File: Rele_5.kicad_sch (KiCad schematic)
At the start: 5 parts

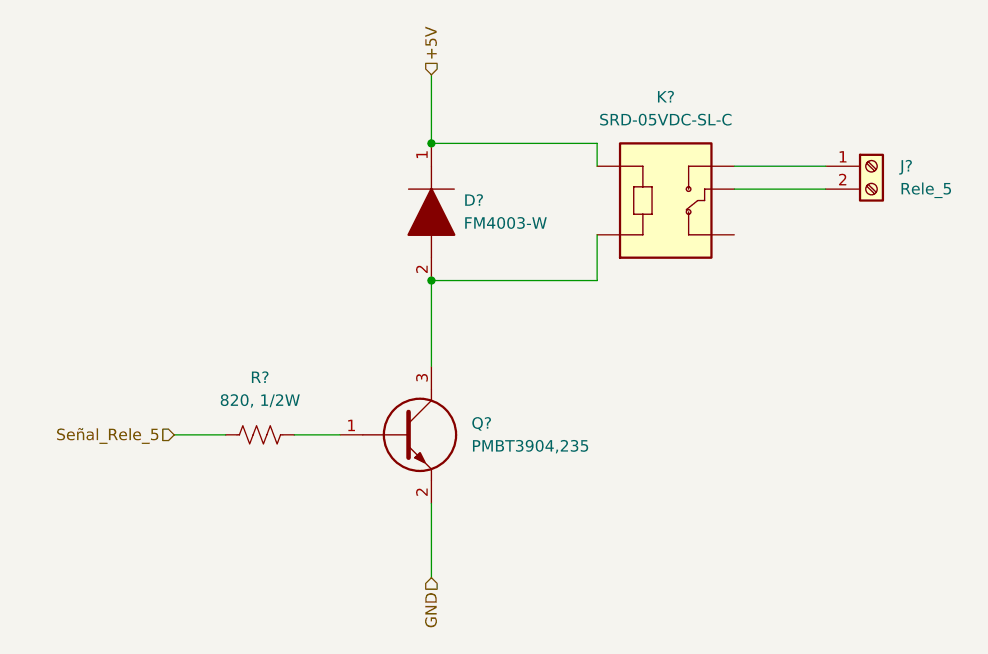
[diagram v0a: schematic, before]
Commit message: Ajuste del esquematico
Se cambio el integrado ESP32 por 2 tiras de pines de 1x15, se quitaron los switches EN y BOOT que ya estan en el NodeMCU, se quito el mutliplexor 74HC y se cablearon las I/O
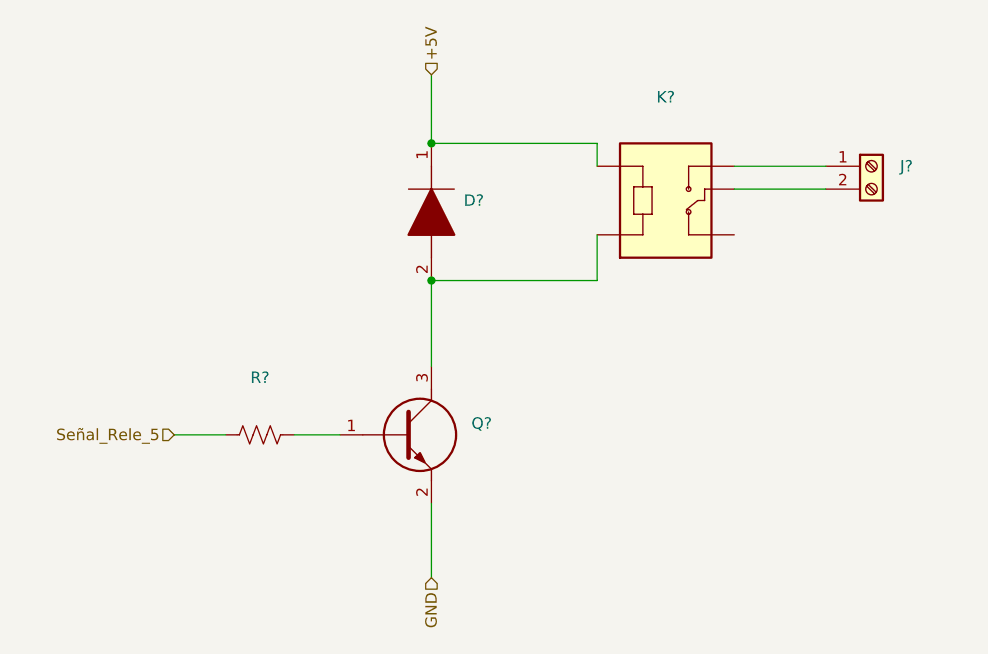
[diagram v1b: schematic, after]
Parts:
- D?: value FM4003-W -> (none); footprint DIOM5025X231N -> (none)
- J?: value Rele_5 -> (none)
- K?: value SRD-05VDC-SL-C -> (none); footprint RELAY_SRD-05VDC-SL-C -> (none)
- Q?: value PMBT3904,235 -> (none); footprint SOT95P230X110-3N -> (none)
- R?: value 820, 1/2W -> (none)
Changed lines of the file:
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@@
     (in_bom yes) (on_board yes) (fields_autoplaced)
     (property "Reference" "K?" (id 0) (at 169.545 70.4342 0))
-    (property "Value" "SRD-05VDC-SL-C" (id 1) (at 169.545 72.9742 0))
-    (property "Footprint" "RELAY_SRD-05VDC-SL-C" (id 2) (at 169.545 80.645 0)
+    (property "Value" "" (id 1) (at 169.545 72.9742 0))
+    (property "Footprint" "" (id 2) (at 169.545 80.645 0)
       (effects (font (size 1.27 1.27)) (justify left bottom) hide)
     )
@@
       (effects (font (size 1.27 1.27)) (justify left))
     )
-    (property "Value" "PMBT3904,235" (id 1) (at 147.955 109.2199 0)
+    (property "Value" "" (id 1) (at 147.955 109.2199 0)
       (effects (font (size 1.27 1.27)) (justify left))
     )
-    (property "Footprint" "SOT95P230X110-3N" (id 2) (at 147.32 111.76 0)
+    (property "Footprint" "" (id 2) (at 147.32 111.76 0)
       (effects (font (size 1.27 1.27)) (justify left) hide)
     )
@@
     (in_bom yes) (on_board yes) (fields_autoplaced)
     (property "Reference" "R?" (id 0) (at 124.46 101.6 90))
-    (property "Value" "820, 1/2W" (id 1) (at 124.46 104.14 90))
+    (property "Value" "" (id 1) (at 124.46 104.14 90))
     (property "Footprint" "" (id 2) (at 124.714 106.934 90)
       (effects (font (size 1.27 1.27)) hide)
@@
       (effects (font (size 1.27 1.27)) (justify left))
     )
-    (property "Value" "Rele_5" (id 1) (at 195.58 80.6449 0)
+    (property "Value" "" (id 1) (at 195.58 80.6449 0)
       (effects (font (size 1.27 1.27)) (justify left))
     )
@@
       (effects (font (size 1.27 1.27)) (justify left))
     )
-    (property "Value" "FM4003-W" (id 1) (at 147.0914 84.4549 90)
+    (property "Value" "" (id 1) (at 147.0914 84.4549 90)
       (effects (font (size 1.27 1.27)) (justify left))
     )
-    (property "Footprint" "DIOM5025X231N" (id 2) (at 143.51 86.995 0)
+    (property "Footprint" "" (id 2) (at 143.51 86.995 0)
       (effects (font (size 1.27 1.27)) (justify left) hide)
     )

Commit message: Modificación de posición de circ. filtrado y circ. de adaptación de tensión
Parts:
- D?, J?, K?, Q?, R?: value (none) -> ~
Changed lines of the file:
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@@
     (in_bom yes) (on_board yes) (fields_autoplaced)
     (property "Reference" "K?" (id 0) (at 169.545 70.4342 0))
-    (property "Value" "" (id 1) (at 169.545 72.9742 0))
+    (property "Value" "~" (id 1) (at 169.545 72.9742 0))
     (property "Footprint" "" (id 2) (at 169.545 80.645 0)
       (effects (font (size 1.27 1.27)) (justify left bottom) hide)
@@
       (effects (font (size 1.27 1.27)) (justify left))
     )
-    (property "Value" "" (id 1) (at 147.955 109.2199 0)
+    (property "Value" "~" (id 1) (at 147.955 109.2199 0)
       (effects (font (size 1.27 1.27)) (justify left))
     )
@@
     (in_bom yes) (on_board yes) (fields_autoplaced)
     (property "Reference" "R?" (id 0) (at 124.46 101.6 90))
-    (property "Value" "" (id 1) (at 124.46 104.14 90))
+    (property "Value" "~" (id 1) (at 124.46 104.14 90))
     (property "Footprint" "" (id 2) (at 124.714 106.934 90)
       (effects (font (size 1.27 1.27)) hide)
@@
       (effects (font (size 1.27 1.27)) (justify left))
     )
-    (property "Value" "" (id 1) (at 195.58 80.6449 0)
+    (property "Value" "~" (id 1) (at 195.58 80.6449 0)
       (effects (font (size 1.27 1.27)) (justify left))
     )
@@
       (effects (font (size 1.27 1.27)) (justify left))
     )
-    (property "Value" "" (id 1) (at 147.0914 84.4549 90)
+    (property "Value" "~" (id 1) (at 147.0914 84.4549 90)
       (effects (font (size 1.27 1.27)) (justify left))
     )

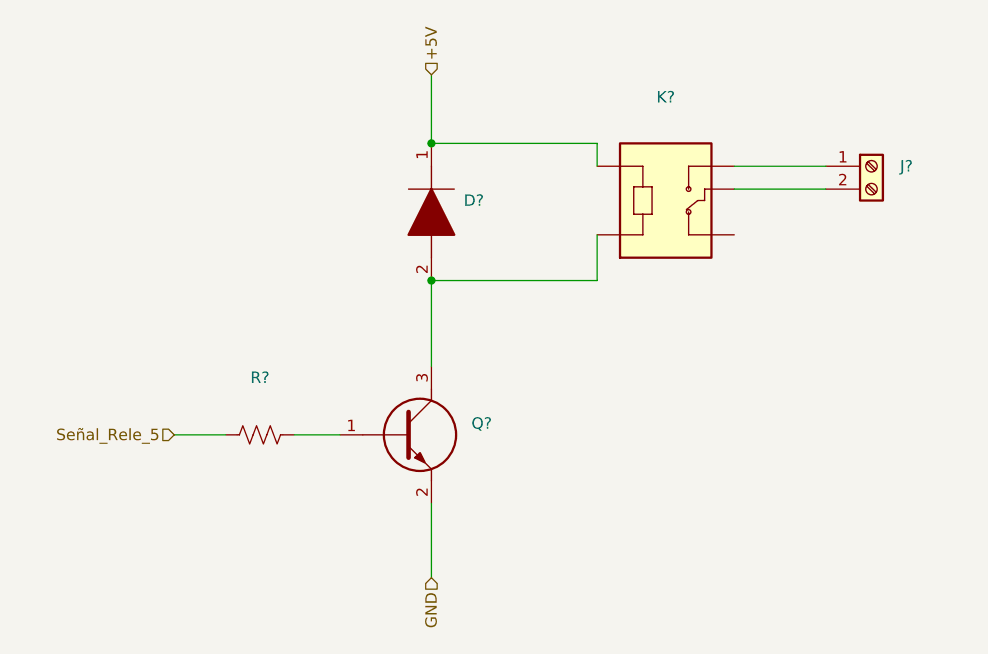
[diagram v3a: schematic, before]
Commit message: Actualización de SCH según placa industrial, y búsqueda de footprints.
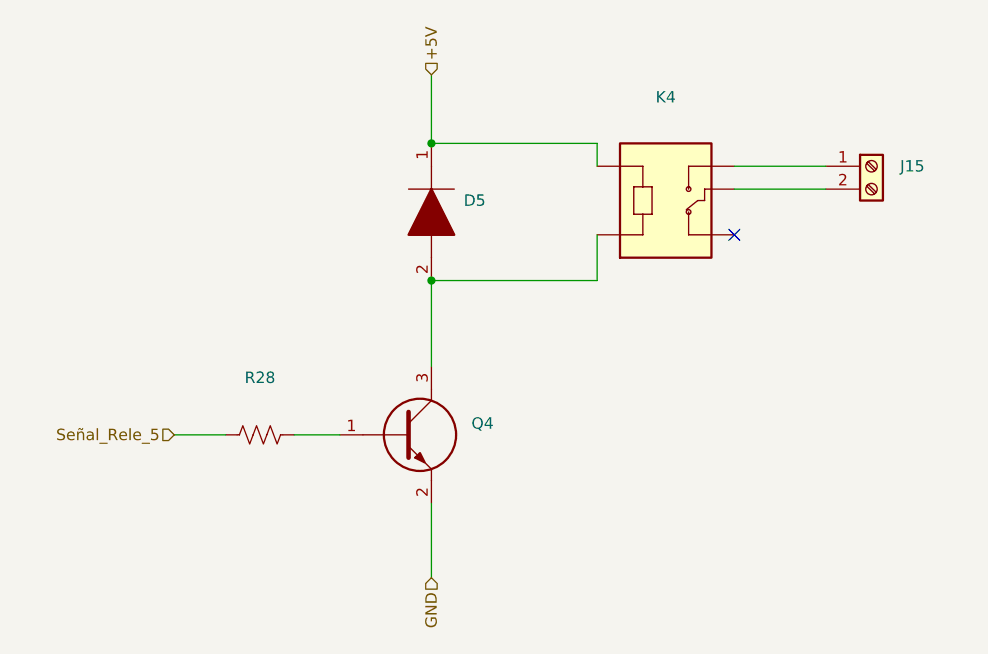
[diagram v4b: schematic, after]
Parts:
- D5: renamed from D?; value ~ -> (none)
- J15: renamed from J?; value ~ -> (none)
- K4: renamed from K?; value ~ -> (none)
- Q4: renamed from Q?; value ~ -> (none)
- R28: renamed from R?; value ~ -> (none)
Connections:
- no-connect marks 0 -> 1
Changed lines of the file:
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@@
   (junction (at 143.51 90.805) (diameter 0) (color 0 0 0 0)
   )
+  (no_connect (at 177.165 85.725))
   (wire (pts (xy 177.165 80.645) (xy 187.325 80.645))
     (stroke (width 0) (type default) (color 0 0 0 0))
@@
   (symbol (lib_id "SRD-05VDC-SL-C:SRD-05VDC-SL-C") (at 169.545 80.645 0) (unit 1)
     (in_bom yes) (on_board yes) (fields_autoplaced)
-    (property "Reference" "K?" (id 0) (at 169.545 70.4342 0))
-    (property "Value" "~" (id 1) (at 169.545 72.9742 0))
+    (property "Reference" "K4" (id 0) (at 169.545 70.4342 0))
+    (property "Value" "" (id 1) (at 169.545 72.9742 0))
     (property "Footprint" "" (id 2) (at 169.545 80.645 0)
       (effects (font (size 1.27 1.27)) (justify left bottom) hide)
@@
   (symbol (lib_id "PMBT3904,235:PMBT3904,235") (at 133.35 107.95 0) (unit 1)
     (in_bom yes) (on_board yes) (fields_autoplaced)
-    (property "Reference" "Q?" (id 0) (at 147.955 106.6799 0)
+    (property "Reference" "Q4" (id 0) (at 147.955 106.6799 0)
       (effects (font (size 1.27 1.27)) (justify left))
     )
-    (property "Value" "~" (id 1) (at 147.955 109.2199 0)
+    (property "Value" "" (id 1) (at 147.955 109.2199 0)
       (effects (font (size 1.27 1.27)) (justify left))
     )
@@
   (symbol (lib_id "Device:R_US") (at 124.46 107.95 90) (unit 1)
     (in_bom yes) (on_board yes) (fields_autoplaced)
-    (property "Reference" "R?" (id 0) (at 124.46 101.6 90))
-    (property "Value" "~" (id 1) (at 124.46 104.14 90))
+    (property "Reference" "R28" (id 0) (at 124.46 101.6 90))
+    (property "Value" "" (id 1) (at 124.46 104.14 90))
     (property "Footprint" "" (id 2) (at 124.714 106.934 90)
       (effects (font (size 1.27 1.27)) hide)
@@
   (symbol (lib_id "Connector:Screw_Terminal_01x02") (at 192.405 78.105 0) (unit 1)
     (in_bom yes) (on_board yes) (fields_autoplaced)
-    (property "Reference" "J?" (id 0) (at 195.58 78.1049 0)
+    (property "Reference" "J15" (id 0) (at 195.58 78.1049 0)
       (effects (font (size 1.27 1.27)) (justify left))
     )
-    (property "Value" "~" (id 1) (at 195.58 80.6449 0)
+    (property "Value" "" (id 1) (at 195.58 80.6449 0)
       (effects (font (size 1.27 1.27)) (justify left))
     )
@@
   (symbol (lib_id "FM4003-W:FM4003-W") (at 143.51 75.565 270) (unit 1)
     (in_bom yes) (on_board yes) (fields_autoplaced)
-    (property "Reference" "D?" (id 0) (at 147.0914 81.9149 90)
+    (property "Reference" "D5" (id 0) (at 147.0914 81.9149 90)
       (effects (font (size 1.27 1.27)) (justify left))
     )
-    (property "Value" "~" (id 1) (at 147.0914 84.4549 90)
+    (property "Value" "" (id 1) (at 147.0914 84.4549 90)
       (effects (font (size 1.27 1.27)) (justify left))
     )

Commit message: Fin de SCH, config de inicio para PCB
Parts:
- D5: value (none) -> FM4003-W; footprint (none) -> FM4003W:DIOM5025X231N
- J15: value (none) -> Rele_5; footprint (none) -> TB002-500-02BE:TB00250002BE
- K4: value (none) -> SRD-05VDC-SL-C; footprint (none) -> SRD-05VDC-SL-C-Version_2:RELAY_SRD-05VDC-SL-C
- Q4: value (none) -> PMBT3904,235; footprint (none) -> PMBT3904,235:SOT95P230X110-3N
- R28: value (none) -> 820, 1/2W; footprint (none) -> Resistor_SMD:R_0805_2012Metric
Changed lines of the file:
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@@
     (in_bom yes) (on_board yes) (fields_autoplaced)
     (property "Reference" "K4" (id 0) (at 169.545 70.4342 0))
-    (property "Value" "" (id 1) (at 169.545 72.9742 0))
-    (property "Footprint" "" (id 2) (at 169.545 80.645 0)
+    (property "Value" "SRD-05VDC-SL-C" (id 1) (at 169.545 72.9742 0))
+    (property "Footprint" "SRD-05VDC-SL-C-Version_2:RELAY_SRD-05VDC-SL-C" (id 2) (at 169.545 80.645 0)
       (effects (font (size 1.27 1.27)) (justify left bottom) hide)
     )
@@
       (effects (font (size 1.27 1.27)) (justify left))
     )
-    (property "Value" "" (id 1) (at 147.955 109.2199 0)
+    (property "Value" "PMBT3904,235" (id 1) (at 147.955 109.2199 0)
       (effects (font (size 1.27 1.27)) (justify left))
     )
-    (property "Footprint" "" (id 2) (at 147.32 111.76 0)
+    (property "Footprint" "PMBT3904,235:SOT95P230X110-3N" (id 2) (at 147.32 111.76 0)
       (effects (font (size 1.27 1.27)) (justify left) hide)
     )
@@
     (in_bom yes) (on_board yes) (fields_autoplaced)
     (property "Reference" "R28" (id 0) (at 124.46 101.6 90))
-    (property "Value" "" (id 1) (at 124.46 104.14 90))
-    (property "Footprint" "" (id 2) (at 124.714 106.934 90)
+    (property "Value" "820, 1/2W" (id 1) (at 124.46 104.14 90))
+    (property "Footprint" "Resistor_SMD:R_0805_2012Metric" (id 2) (at 124.714 106.934 90)
       (effects (font (size 1.27 1.27)) hide)
     )
@@
       (effects (font (size 1.27 1.27)) (justify left))
     )
-    (property "Value" "" (id 1) (at 195.58 80.6449 0)
+    (property "Value" "Rele_5" (id 1) (at 195.58 80.6449 0)
       (effects (font (size 1.27 1.27)) (justify left))
     )
-    (property "Footprint" "" (id 2) (at 192.405 78.105 0)
+    (property "Footprint" "TB002-500-02BE:TB00250002BE" (id 2) (at 192.405 78.105 0)
       (effects (font (size 1.27 1.27)) hide)
     )
@@
       (effects (font (size 1.27 1.27)) (justify left))
     )
-    (property "Value" "" (id 1) (at 147.0914 84.4549 90)
+    (property "Value" "FM4003-W" (id 1) (at 147.0914 84.4549 90)
       (effects (font (size 1.27 1.27)) (justify left))
     )
-    (property "Footprint" "" (id 2) (at 143.51 86.995 0)
+    (property "Footprint" "FM4003W:DIOM5025X231N" (id 2) (at 143.51 86.995 0)
       (effects (font (size 1.27 1.27)) (justify left) hide)
     )

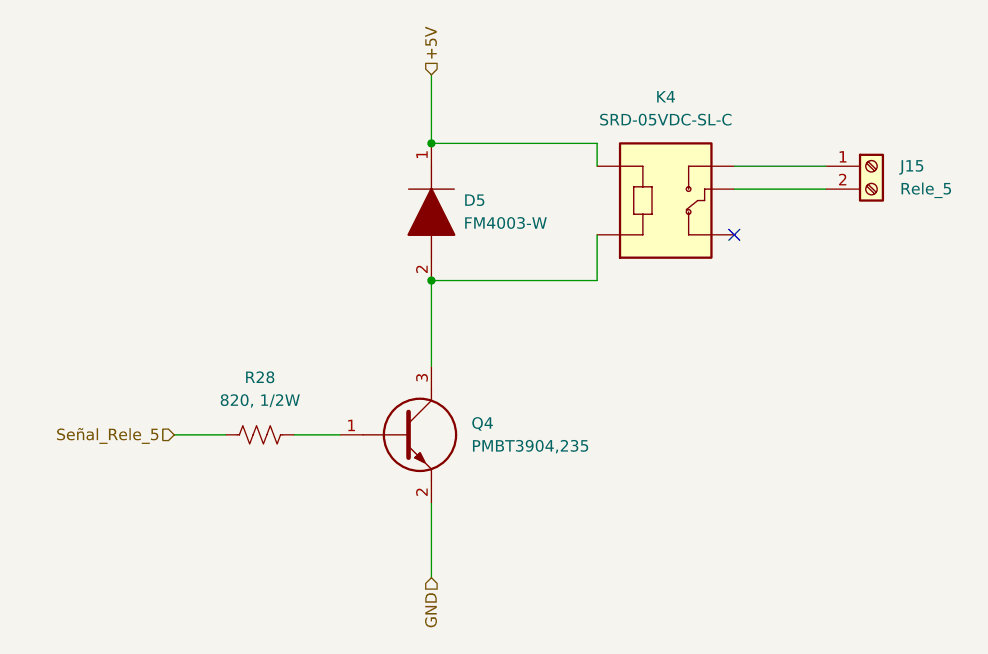
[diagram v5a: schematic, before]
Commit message: Cambios en SCH y PCB.
Se cambio el adaptador de nivel 5-3,3V por un circuito con MOSFET 2N7002, dado que ya no hay stock del NXB. Se modificó el footprint del expansor I/O por uno thorugh-hole.
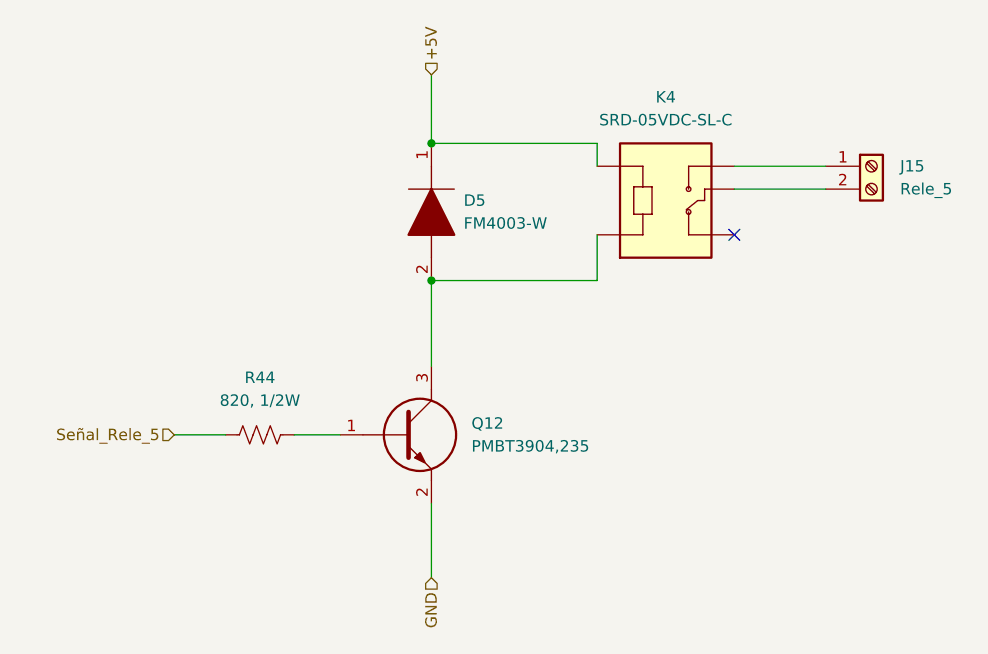
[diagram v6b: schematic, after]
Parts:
- renumbered Q4 to Q12, R28 to R44
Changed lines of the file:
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@@
   (symbol (lib_id "PMBT3904,235:PMBT3904,235") (at 133.35 107.95 0) (unit 1)
     (in_bom yes) (on_board yes) (fields_autoplaced)
-    (property "Reference" "Q4" (id 0) (at 147.955 106.6799 0)
+    (property "Reference" "Q12" (id 0) (at 147.955 106.6799 0)
       (effects (font (size 1.27 1.27)) (justify left))
     )
@@
   (symbol (lib_id "Device:R_US") (at 124.46 107.95 90) (unit 1)
     (in_bom yes) (on_board yes) (fields_autoplaced)
-    (property "Reference" "R28" (id 0) (at 124.46 101.6 90))
+    (property "Reference" "R44" (id 0) (at 124.46 101.6 90))
     (property "Value" "820, 1/2W" (id 1) (at 124.46 104.14 90))
     (property "Footprint" "Resistor_SMD:R_0805_2012Metric" (id 2) (at 124.714 106.934 90)

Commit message: Se finalizó con el PCB del prototipo.
Dado que se buscó a toda costa que el PCB fuera de 1 capa, en varios puntos del circuito se tuvieron que agregar pin headers individuales para conectar a 3V3 y GND, junto con tiras de pin headers. Cada una de estas se conectara luego entre si mediante cables.

Tambien se generaron los archivos Gerber y BOM.
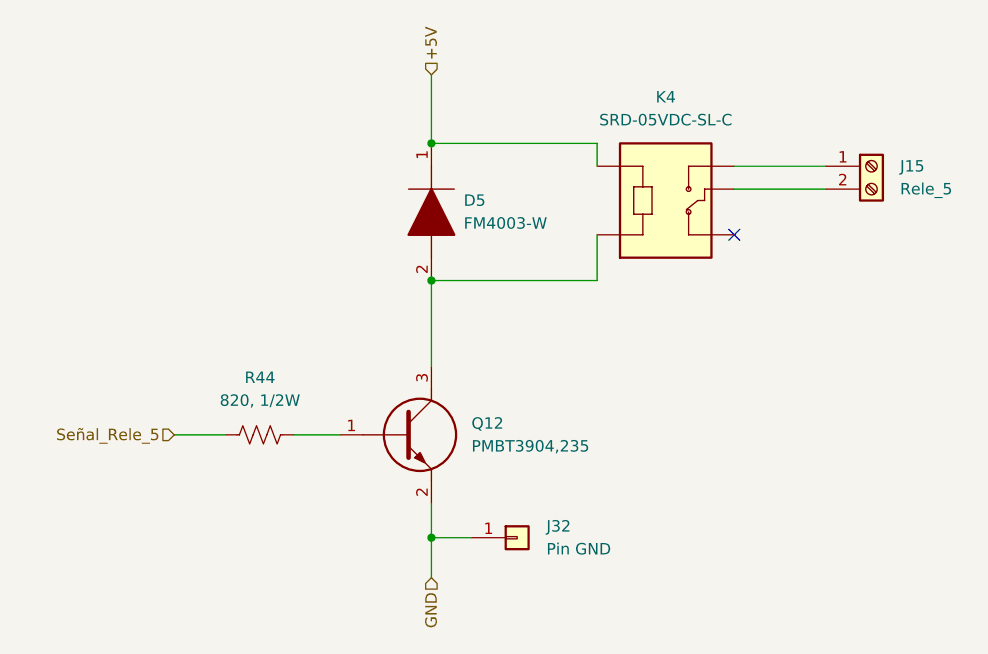
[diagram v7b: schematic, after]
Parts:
- added J32: Pin GND, Connector_PinHeader_2.54mm:PinHeader_1x01_P2.54mm_Vertical, symbol Connector_Generic:Conn_01x01
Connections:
- net GND: now also J32.1 (Pin_1)
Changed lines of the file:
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@@
   (junction (at 143.51 90.805) (diameter 0) (color 0 0 0 0)
   )
+  (junction (at 143.51 119.38) (diameter 0) (color 0 0 0 0)
+  )
   (no_connect (at 177.165 85.725))
+  (wire (pts (xy 143.51 119.38) (xy 147.955 119.38))
+    (stroke (width 0) (type default) (color 0 0 0 0))
+  )
   (wire (pts (xy 177.165 80.645) (xy 187.325 80.645))
     (stroke (width 0) (type default) (color 0 0 0 0))
@@
     (stroke (width 0) (type default) (color 0 0 0 0))
   )
-  (wire (pts (xy 143.51 115.57) (xy 143.51 123.825))
+  (wire (pts (xy 143.51 115.57) (xy 143.51 119.38))
     (stroke (width 0) (type default) (color 0 0 0 0))
   )
@@
   )
   (wire (pts (xy 143.51 90.805) (xy 161.925 90.805))
+    (stroke (width 0) (type default) (color 0 0 0 0))
+  )
+  (wire (pts (xy 143.51 119.38) (xy 143.51 123.825))
     (stroke (width 0) (type default) (color 0 0 0 0))
   )
@@
     (pin "2")
   )
+  (symbol (lib_id "Connector_Generic:Conn_01x01") (at 153.035 119.38 0) (unit 1)
+    (in_bom yes) (on_board yes) (fields_autoplaced)
+    (property "Reference" "J32" (id 0) (at 156.2862 118.1099 0)
+      (effects (font (size 1.27 1.27)) (justify left))
+    )
+    (property "Value" "Pin GND" (id 1) (at 156.2862 120.6499 0)
+      (effects (font (size 1.27 1.27)) (justify left))
+    )
+    (property "Footprint" "Connector_PinHeader_2.54mm:PinHeader_1x01_P2.54mm_Vertical" (id 2) (at 153.035 119.38 0)
+      (effects (font (size 1.27 1.27)) hide)
+    )
+    (property "Datasheet" "~" (id 3) (at 153.035 119.38 0)
+      (effects (font (size 1.27 1.27)) hide)
+    )
+    (pin "1")
+  )
   (symbol (lib_id "FM4003-W:FM4003-W") (at 143.51 75.565 270) (unit 1)
